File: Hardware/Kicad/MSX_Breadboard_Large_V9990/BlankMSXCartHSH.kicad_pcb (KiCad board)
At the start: 2 copper layers, 100.1 x 131.3 mm, 58 parts, among them CN1 MSXBUS, U1 V9990, U2 KM428C256, U3 KM428C256, U4 LMH1980, U5 CXA2075M

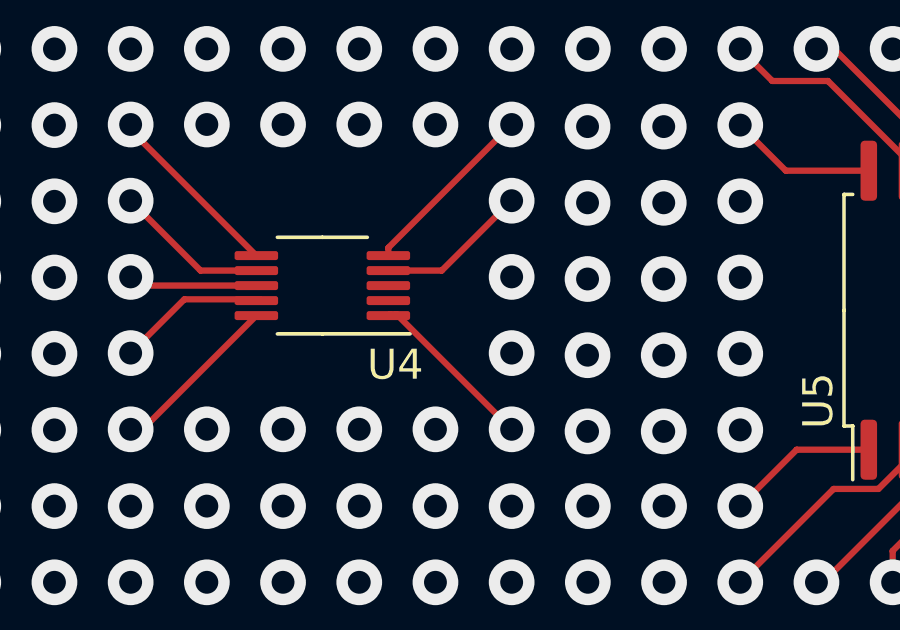
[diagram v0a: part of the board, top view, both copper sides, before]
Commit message: Small fix to the prototype MSX_Breadboard_Large_V9990 board
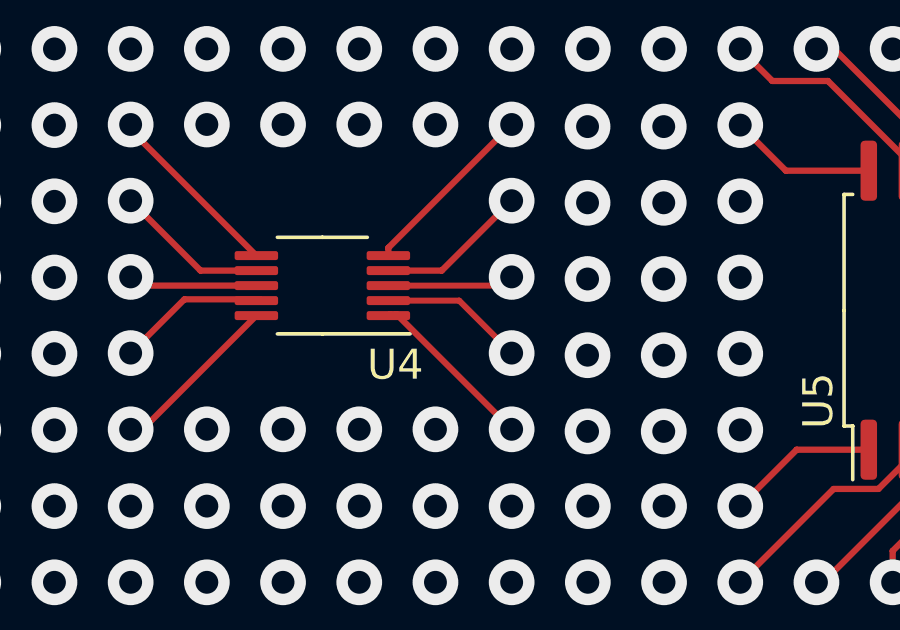
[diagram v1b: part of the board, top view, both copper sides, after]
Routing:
- net (no net): track 0.00 -> 9.06 mm
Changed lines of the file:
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@@
     (effects (font (size 1 1) (thickness 0.15)))
   )
+  (segment (start 85.28 117.2) (end 87.64 117.2) (width 0.2) (layer "F.Cu") (net 0))
+  (segment (start 89.1 116.7) (end 89.39 116.41) (width 0.2) (layer "F.Cu") (net 0))
+  (segment (start 85.28 116.7) (end 89.1 116.7) (width 0.2) (layer "F.Cu") (net 0))
+  (segment (start 87.64 117.2) (end 89.39 118.95) (width 0.2) (layer "F.Cu") (net 0))
   (via (at 142.8 93.5) (size 1.524) (drill 0.762) (layers "F.Cu" "B.Cu") (net 0))
   (via (at 86.85 124.05) (size 1.524) (drill 0.762) (layers "F.Cu" "B.Cu") (net 0))
@@
   (via (at 74.15 124.05) (size 1.524) (drill 0.762) (layers "F.Cu" "B.Cu") (net 0))
   (via (at 97.01 146.91) (size 1.524) (drill 0.762) (layers "F.Cu" "B.Cu") (net 0))
-  (via (at 135.11 154.53) (size 1.524) (drill 0.762) (layers "F.Cu" "B.Cu") (net 0))
+  (via (at 135.11 154.53) (size 1.524) (drill 0.762) (layers "F.Cu" "B.Cu") (remove_unused_layers) (keep_end_layers) (free) (net 0))
   (via (at 119.87 116.43) (size 1.524) (drill 0.762) (layers "F.Cu" "B.Cu") (net 0))
   (via (at 137.65 146.91) (size 1.524) (drill 0.762) (layers "F.Cu" "B.Cu") (net 0))
